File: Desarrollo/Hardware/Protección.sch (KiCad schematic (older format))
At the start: 51 parts, among them J1 Entradas Analógicas, U1 TPD2E001, U15 TPD2E001, U2 TPD2E001, U3 TPD2E001, U4 TPD2E001, U5 TPD2E001, U6 TPD2E001, U7 TPD2E001, U8 TPD2E001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

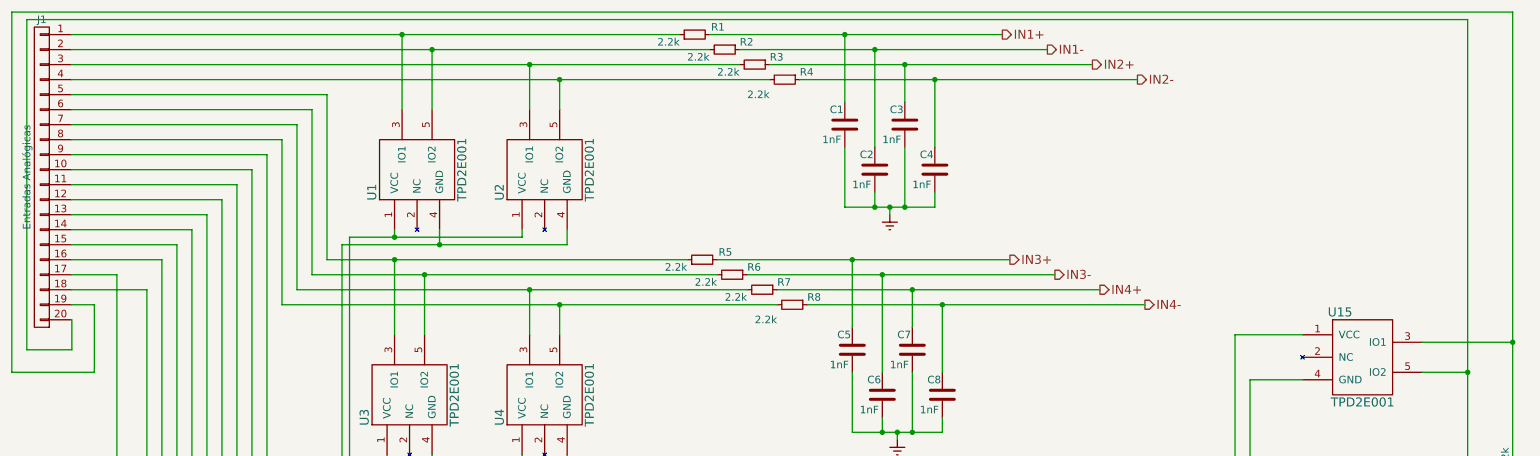
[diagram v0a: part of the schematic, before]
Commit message: Mejora de ubicación de componentes y nuevo ruteo desde 0. Disminución notable de cantidad de vías. Diseño (casi) final. REVISAR.
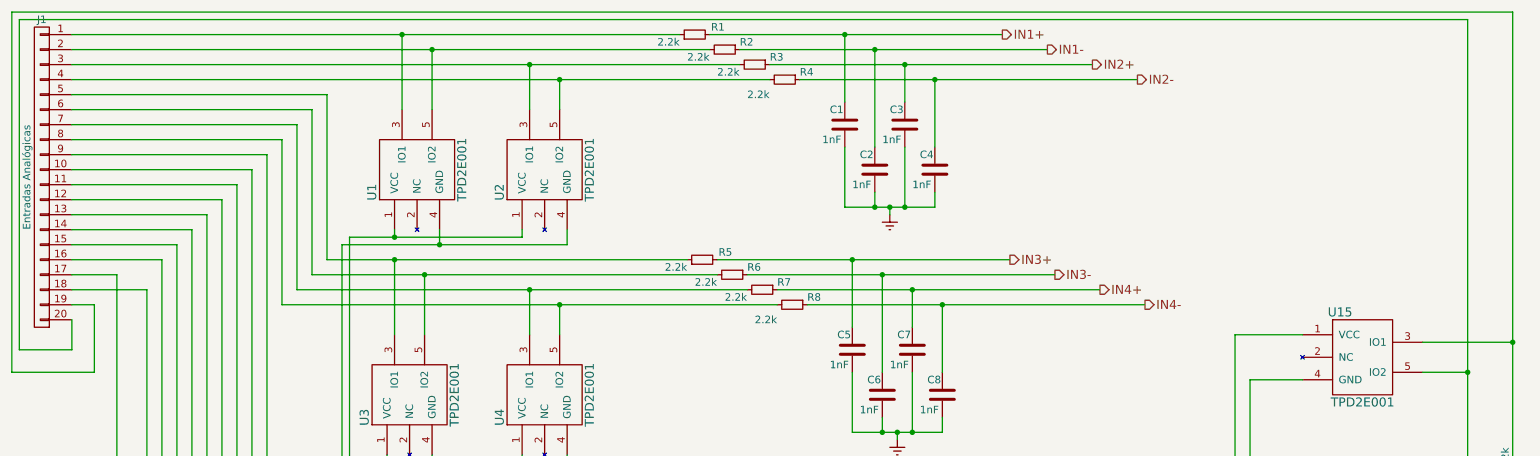
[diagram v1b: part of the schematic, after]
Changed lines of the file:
@@
 	1100 2500 1100 2950
 Wire Wire Line
-	950  2600 950  2800
+	950  2800 950  2600
 Wire Wire Line
-	10250 600  650  600
+	600  600  10250 600
 Wire Wire Line
-	650  600  650  2800
-Wire Wire Line
-	650  2800 950  2800
+	600  2800 950  2800
 Wire Wire Line
 	1100 2950 550  2950
@@
 Wire Wire Line
 	550  550  10550 550
+Wire Wire Line
+	600  2800 600  600
 $EndSCHEMATC

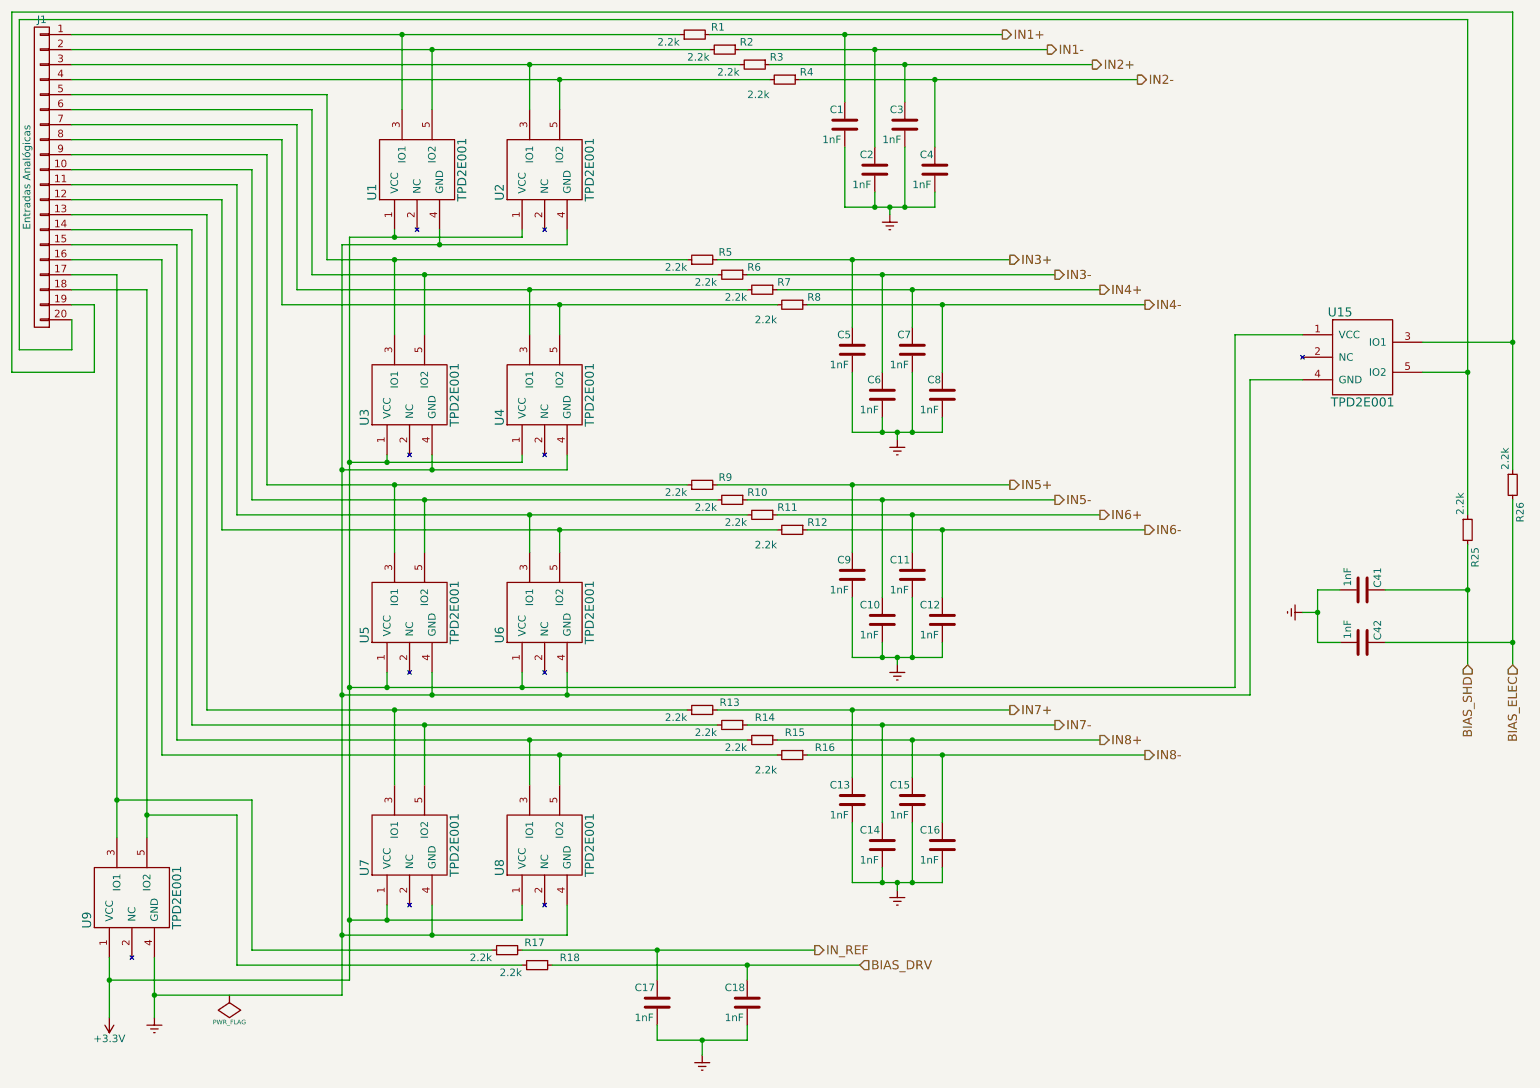
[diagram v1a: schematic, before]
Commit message: Actualización de esquemático, se completaron campos de "Hoja de dato" y "Código Digikey" para cada componente. Se completaron los rótulos de hojas. Versión Final de PCB. Actualización de tamaño de pistas y redimensión de zonas de relleno. Lista de Materiales actualizada en carpeta "Documentación".
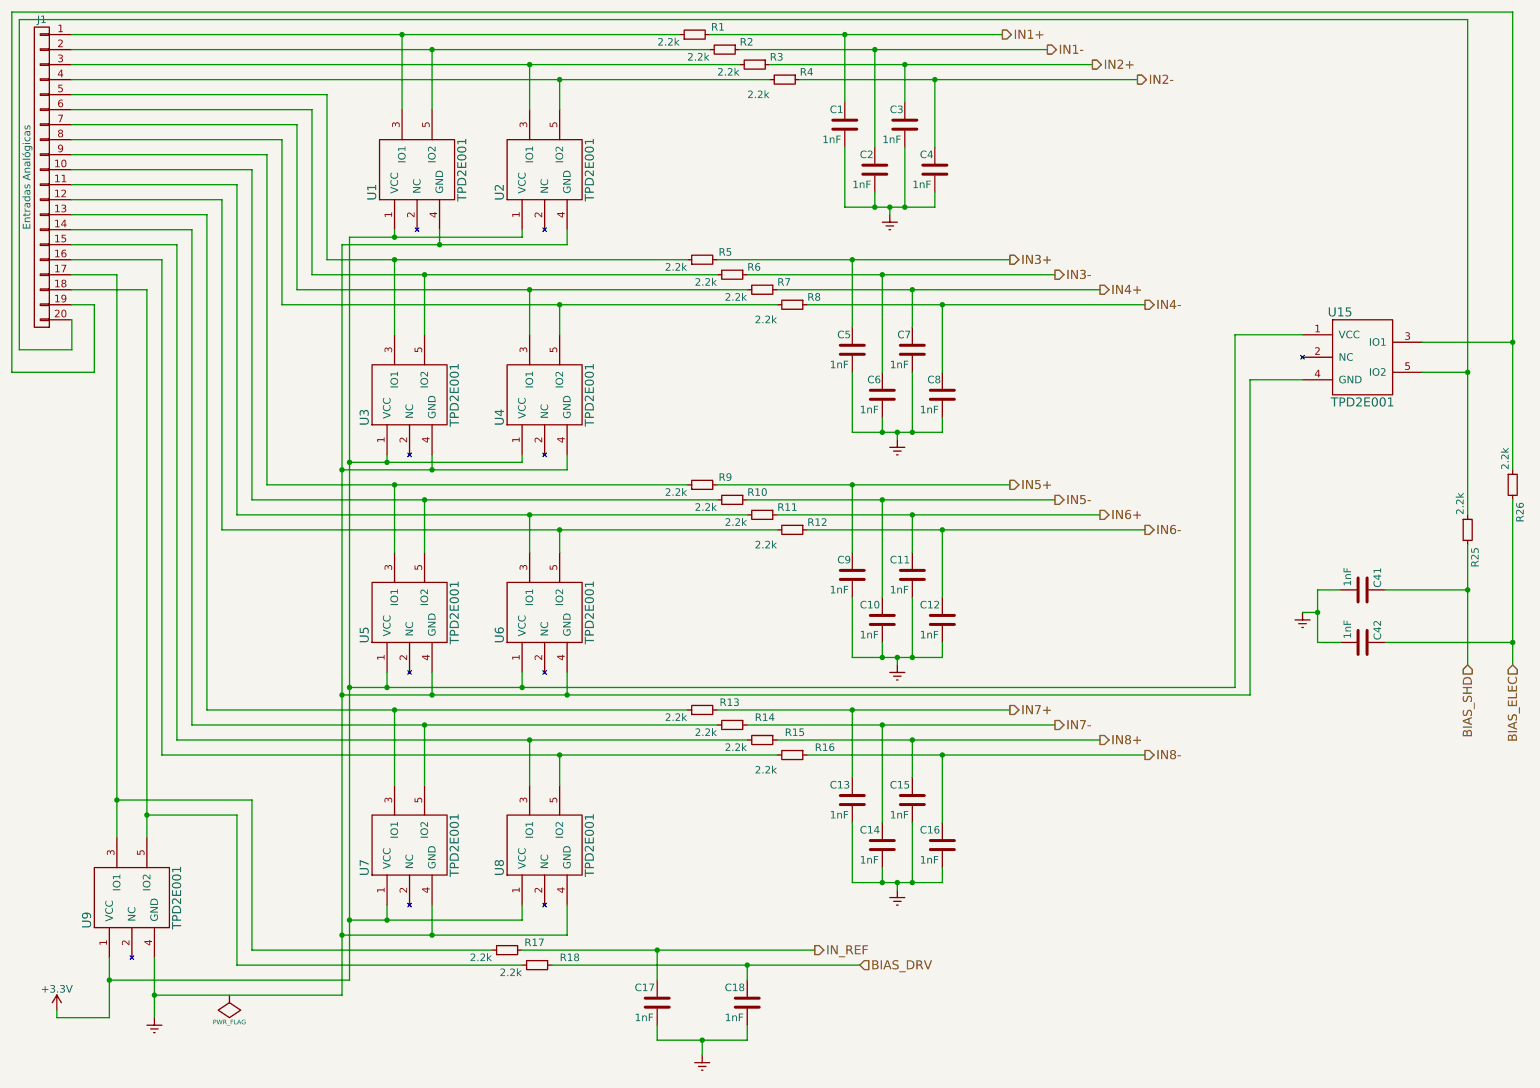
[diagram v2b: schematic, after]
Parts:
- C1, C10, C11, C12, C13, C14, C15, C16, C17, C18, C2, C3, C4, C41, C42, C5, C6, C7, C8, C9: Código Digikey (none) -> 399-1147-1-ND
- J1: Código Digikey (none) -> 3M9455-ND
- R1, R10, R11, R12, R13, R14, R15, R16, R17, R18, R2, R25, R26, R3, R4, R6, R7, R8, R9: Código Digikey (none) -> 311-2.2KARCT-ND
- U1, U15, U2, U3, U4, U5, U6, U7, U8, U9: Código Digikey (none) -> 296-21883-1-ND

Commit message: Modificaciones basadas en nuevas revisiones. Se agregaron bypass en ADuMs. Inclusión de símbolos de "PONCHO" y "OPEN HARDWARE". Algunos cambios estéticos de pistas y otros funcionales. Unificación de vías. Extensión de capas de cobre en sector de aislación. Mejora de stitching. Quedaron revisiones pendientes que serán consultadas.
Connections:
- net Earth renamed DGND
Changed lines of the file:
@@
 $EndComp
 $Comp
-L Earth #PWR02
+L DGND #PWR02
 U 1 1 57CB2925
 P 1500 7250
 F 0 "#PWR02" H 1500 7000 50  0001 C CNN
-F 1 "Earth" H 1500 7100 50  0001 C CNN
+F 1 "DGND" H 1500 7100 50  0001 C CNN
 F 2 "" H 1500 7250 50  0000 C CNN
 F 3 "" H 1500 7250 50  0000 C CNN
@@
 $EndComp
 $Comp
-L Earth #PWR03
+L DGND #PWR03
 U 1 1 57CB2C47
 P 5150 7500
 F 0 "#PWR03" H 5150 7250 50  0001 C CNN
-F 1 "Earth" H 5150 7350 50  0001 C CNN
+F 1 "DGND" H 5150 7350 50  0001 C CNN
 F 2 "" H 5150 7500 50  0000 C CNN
 F 3 "" H 5150 7500 50  0000 C CNN
@@
 $EndComp
 $Comp
-L Earth #PWR04
+L DGND #PWR04
 U 1 1 57CB2CB7
 P 6450 6400
 F 0 "#PWR04" H 6450 6150 50  0001 C CNN
-F 1 "Earth" H 6450 6250 50  0001 C CNN
+F 1 "DGND" H 6450 6250 50  0001 C CNN
 F 2 "" H 6450 6400 50  0000 C CNN
 F 3 "" H 6450 6400 50  0000 C CNN
@@
 $EndComp
 $Comp
-L Earth #PWR05
+L DGND #PWR05
 U 1 1 57CB2D27
 P 6450 4900
 F 0 "#PWR05" H 6450 4650 50  0001 C CNN
-F 1 "Earth" H 6450 4750 50  0001 C CNN
+F 1 "DGND" H 6450 4750 50  0001 C CNN
 F 2 "" H 6450 4900 50  0000 C CNN
 F 3 "" H 6450 4900 50  0000 C CNN
@@
 $EndComp
 $Comp
-L Earth #PWR06
+L DGND #PWR06
 U 1 1 57CB3077
 P 6400 1900
 F 0 "#PWR06" H 6400 1650 50  0001 C CNN
-F 1 "Earth" H 6400 1750 50  0001 C CNN
+F 1 "DGND" H 6400 1750 50  0001 C CNN
 F 2 "" H 6400 1900 50  0000 C CNN
 F 3 "" H 6400 1900 50  0000 C CNN
@@
 $EndComp
 $Comp
-L Earth #PWR07
+L DGND #PWR07
 U 1 1 57CB30E7
 P 6450 3400
 F 0 "#PWR07" H 6450 3150 50  0001 C CNN
-F 1 "Earth" H 6450 3250 50  0001 C CNN
+F 1 "DGND" H 6450 3250 50  0001 C CNN
 F 2 "" H 6450 3400 50  0000 C CNN
 F 3 "" H 6450 3400 50  0000 C CNN
@@
 Connection ~ 4250 5100
 $Comp
-L Earth #PWR09
+L DGND #PWR09
 U 1 1 57D08E33
 P 9150 4550
 F 0 "#PWR09" H 9150 4300 50  0001 C CNN
-F 1 "Earth" H 9150 4400 50  0001 C CNN
+F 1 "DGND" H 9150 4400 50  0001 C CNN
 F 2 "" H 9150 4550 50  0000 C CNN
 F 3 "" H 9150 4550 50  0000 C CNN

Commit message: Nueva actualización. Intercambio de tierras GNDA por DGND en hoja esquemático "Aislación". Ídem en hoja de "Protección". Además se hizo visible el nombre de la tierra digital DGND que no figuraba. Revisión FINAL. Cambios estéticos en ubicación de algunas pistas del PCB.
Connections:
- net DGND renamed GNDA
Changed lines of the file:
@@
-$EndComp
-$Comp
-L DGND #PWR02
-U 1 1 57CB2925
-P 1500 7250
-F 0 "#PWR02" H 1500 7000 50  0001 C CNN
-F 1 "DGND" H 1500 7100 50  0001 C CNN
-F 2 "" H 1500 7250 50  0000 C CNN
-F 3 "" H 1500 7250 50  0000 C CNN
-	1    1500 7250
-	1    0    0    -1
-$EndComp
-$Comp
-L DGND #PWR03
-U 1 1 57CB2C47
-P 5150 7500
-F 0 "#PWR03" H 5150 7250 50  0001 C CNN
-F 1 "DGND" H 5150 7350 50  0001 C CNN
-F 2 "" H 5150 7500 50  0000 C CNN
-F 3 "" H 5150 7500 50  0000 C CNN
-	1    5150 7500
-	1    0    0    -1
-$EndComp
-$Comp
-L DGND #PWR04
-U 1 1 57CB2CB7
-P 6450 6400
-F 0 "#PWR04" H 6450 6150 50  0001 C CNN
-F 1 "DGND" H 6450 6250 50  0001 C CNN
-F 2 "" H 6450 6400 50  0000 C CNN
-F 3 "" H 6450 6400 50  0000 C CNN
-	1    6450 6400
-	1    0    0    -1
-$EndComp
-$Comp
-L DGND #PWR05
-U 1 1 57CB2D27
-P 6450 4900
-F 0 "#PWR05" H 6450 4650 50  0001 C CNN
-F 1 "DGND" H 6450 4750 50  0001 C CNN
-F 2 "" H 6450 4900 50  0000 C CNN
-F 3 "" H 6450 4900 50  0000 C CNN
-	1    6450 4900
-	1    0    0    -1
-$EndComp
-$Comp
-L DGND #PWR06
-U 1 1 57CB3077
-P 6400 1900
-F 0 "#PWR06" H 6400 1650 50  0001 C CNN
-F 1 "DGND" H 6400 1750 50  0001 C CNN
-F 2 "" H 6400 1900 50  0000 C CNN
-F 3 "" H 6400 1900 50  0000 C CNN
-	1    6400 1900
-	1    0    0    -1
-$EndComp
-$Comp
-L DGND #PWR07
-U 1 1 57CB30E7
-P 6450 3400
-F 0 "#PWR07" H 6450 3150 50  0001 C CNN
-F 1 "DGND" H 6450 3250 50  0001 C CNN
-F 2 "" H 6450 3400 50  0000 C CNN
-F 3 "" H 6450 3400 50  0000 C CNN
-	1    6450 3400
-	1    0    0    -1
 $EndComp
 $Comp
@@
 	8800 3000 8800 5100
 Connection ~ 4250 5100
-$Comp
-L DGND #PWR09
-U 1 1 57D08E33
-P 9150 4550
-F 0 "#PWR09" H 9150 4300 50  0001 C CNN
-F 1 "DGND" H 9150 4400 50  0001 C CNN
-F 2 "" H 9150 4550 50  0000 C CNN
-F 3 "" H 9150 4550 50  0000 C CNN
-	1    9150 4550
-	1    0    0    -1
-$EndComp
 Wire Wire Line
 	9150 4550 9250 4550
@@
 	0    -1   -1   0
 $EndComp
+$Comp
+L GNDA #PWR?
+U 1 1 580E2DEF
+P 6400 1900
+F 0 "#PWR?" H 6400 1900 40  0001 C CNN
+F 1 "GNDA" H 6400 1800 40  0000 C CNN
+F 2 "" H 6400 1900 60  0000 C CNN
+F 3 "" H 6400 1900 60  0000 C CNN
+	1    6400 1900
+	1    0    0    -1
+$EndComp
+$Comp
+L GNDA #PWR?
+U 1 1 580E4132
+P 6450 3400
+F 0 "#PWR?" H 6450 3400 40  0001 C CNN
+F 1 "GNDA" H 6450 3300 40  0000 C CNN
+F 2 "" H 6450 3400 60  0000 C CNN
+F 3 "" H 6450 3400 60  0000 C CNN
+	1    6450 3400
+	1    0    0    -1
+$EndComp
+$Comp
+L GNDA #PWR?
+U 1 1 580E41D6
+P 6450 4900
+F 0 "#PWR?" H 6450 4900 40  0001 C CNN
+F 1 "GNDA" H 6450 4800 40  0000 C CNN
+F 2 "" H 6450 4900 60  0000 C CNN
+F 3 "" H 6450 4900 60  0000 C CNN
+	1    6450 4900
+	1    0    0    -1
+$EndComp
+$Comp
+L GNDA #PWR?
+U 1 1 580E427A
+P 6450 6400
+F 0 "#PWR?" H 6450 6400 40  0001 C CNN
+F 1 "GNDA" H 6450 6300 40  0000 C CNN
+F 2 "" H 6450 6400 60  0000 C CNN
+F 3 "" H 6450 6400 60  0000 C CNN
+	1    6450 6400
+	1    0    0    -1
+$EndComp
+$Comp
+L GNDA #PWR?
+U 1 1 580E431E
+P 9150 4600
+F 0 "#PWR?" H 9150 4600 40  0001 C CNN
+F 1 "GNDA" H 9150 4500 40  0000 C CNN
+F 2 "" H 9150 4600 60  0000 C CNN
+F 3 "" H 9150 4600 60  0000 C CNN
+	1    9150 4600
+	1    0    0    -1
+$EndComp
+Wire Wire Line
+	9150 4550 9150 4600
+$Comp
+L GNDA #PWR?
+U 1 1 580E44F9
+P 1500 7250
+F 0 "#PWR?" H 1500 7250 40  0001 C CNN
+F 1 "GNDA" H 1500 7150 40  0000 C CNN
+F 2 "" H 1500 7250 60  0000 C CNN
+F 3 "" H 1500 7250 60  0000 C CNN
+	1    1500 7250
+	1    0    0    -1
+$EndComp
+$Comp
+L GNDA #PWR?
+U 1 1 580E459D
+P 5150 7500
+F 0 "#PWR?" H 5150 7500 40  0001 C CNN
+F 1 "GNDA" H 5150 7400 40  0000 C CNN
+F 2 "" H 5150 7500 60  0000 C CNN
+F 3 "" H 5150 7500 60  0000 C CNN
+	1    5150 7500
+	1    0    0    -1
+$EndComp
 $EndSCHEMATC
